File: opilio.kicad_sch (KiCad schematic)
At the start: 24 parts, among them J1 Conn_01x04_Male, SW1 TS-1077S-01726, SW2 TS-1077S-01726, U1 STM32F103C8T6, Y1 YST310S 32.768KHz, Y2 TAXM8M4RFDCET2T

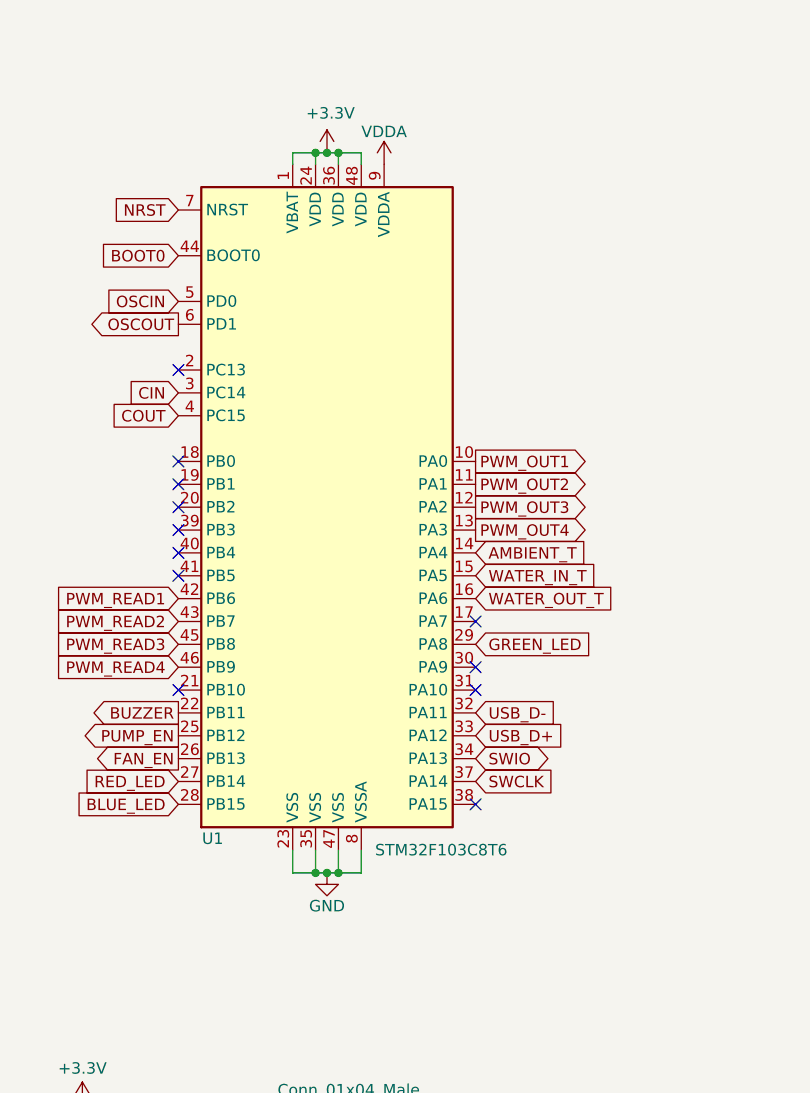
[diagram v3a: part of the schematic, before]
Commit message: wip migrate to kicad 7
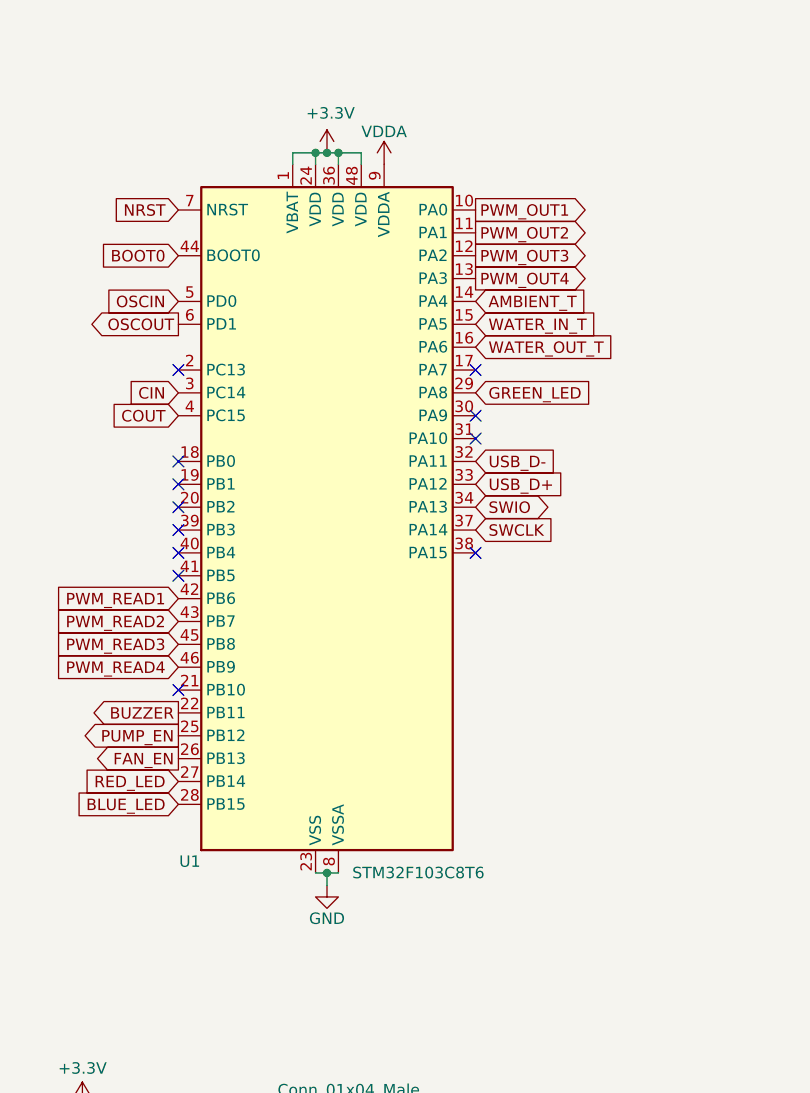
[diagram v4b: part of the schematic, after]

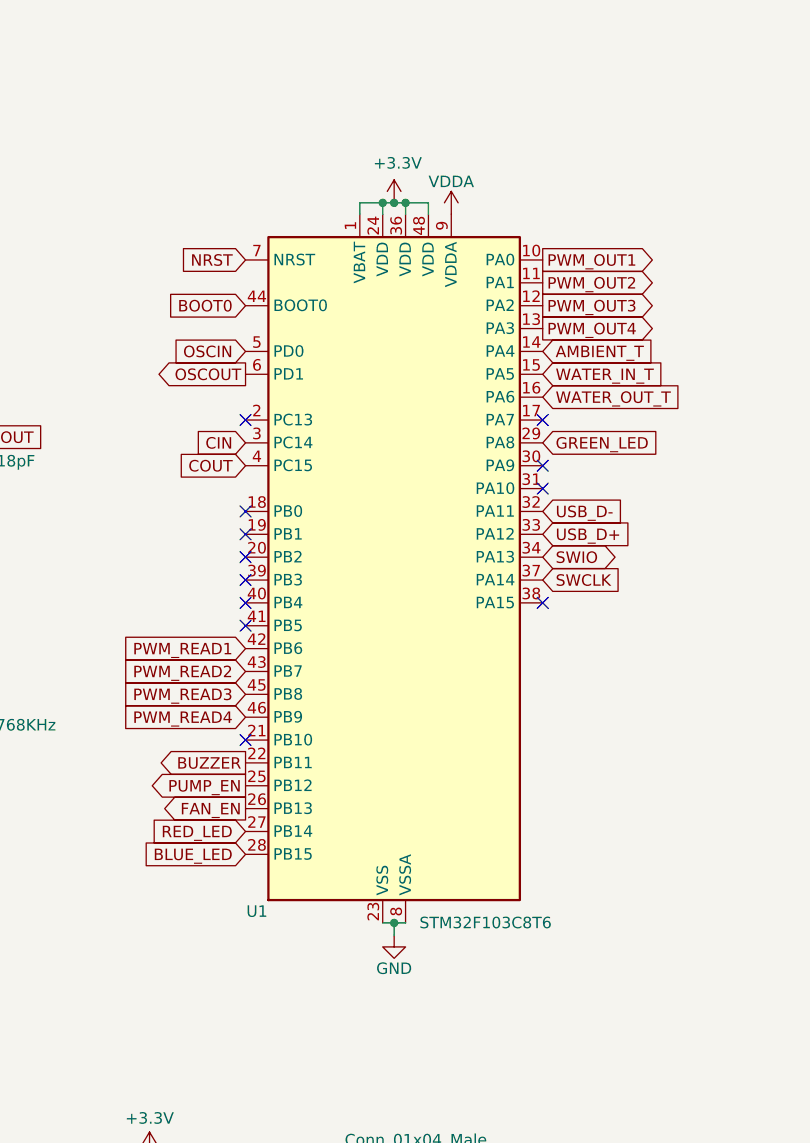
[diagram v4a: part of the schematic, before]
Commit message: migrated to kicad-7
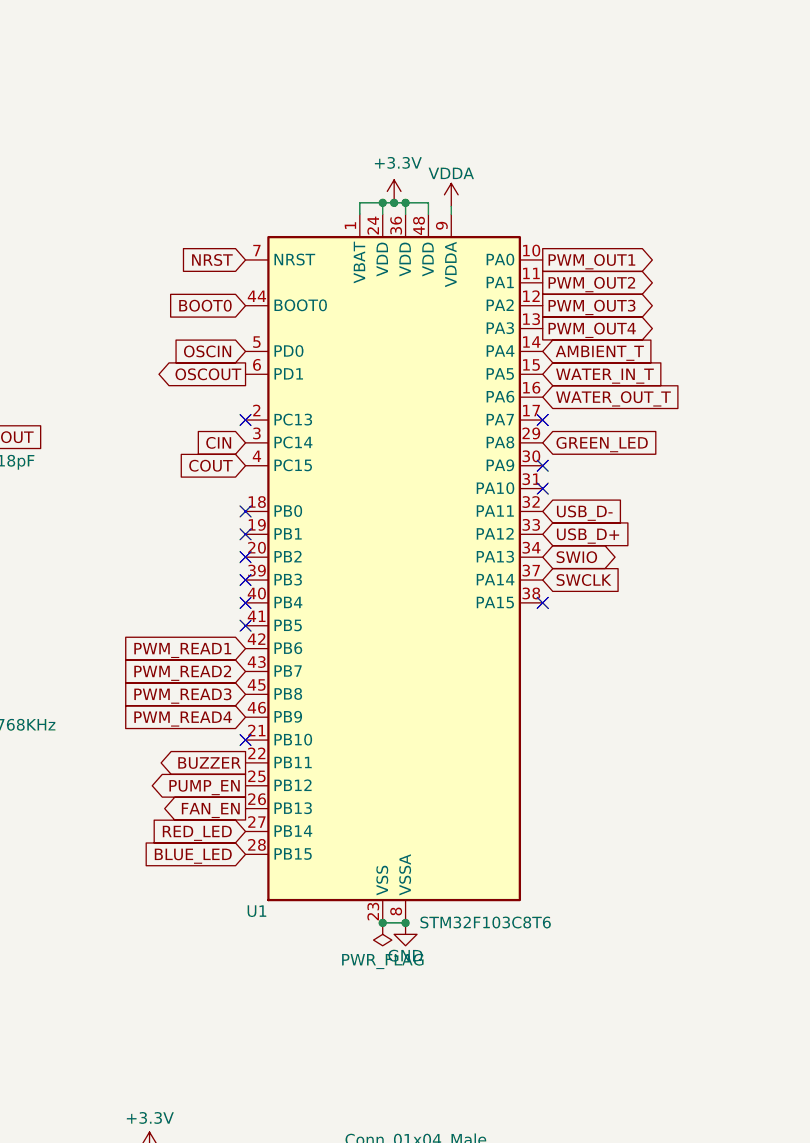
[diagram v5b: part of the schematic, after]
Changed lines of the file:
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@@
   (junction (at 118.999 61.976) (diameter 0) (color 0 0 0 0)
   )
+  (junction (at 118.999 141.986) (diameter 0) (color 0 0 0 0)
+  )
   (junction (at 51.181 118.999) (diameter 0) (color 0 0 0 0)
   )
   (junction (at 103.124 27.305) (diameter 0) (color 0 0 0 0)
   )
+  (junction (at 116.459 141.986) (diameter 0) (color 0 0 0 0)
+  )
   (junction (at 26.162 82.677) (diameter 0) (color 0 0 0 0)
   )
@@
   )
   (junction (at 29.591 51.181) (diameter 0) (color 0 0 0 0)
-  )
-  (junction (at 117.729 141.986) (diameter 0) (color 0 0 0 0)
   )
   (junction (at 31.242 78.613) (diameter 0) (color 0 0 0 0)
@@
     (stroke (width 0) (type default))
   )
-  (wire (pts (xy 116.459 141.986) (xy 117.729 141.986))
+  (wire (pts (xy 116.459 141.986) (xy 118.999 141.986))
     (stroke (width 0) (type default))
   )
@@
     (stroke (width 0) (type default))
   )
-  (wire (pts (xy 117.729 143.383) (xy 117.729 141.986))
-    (stroke (width 0) (type default))
-  )
   (wire (pts (xy 34.163 70.104) (xy 34.163 72.898))
     (stroke (width 0) (type default))
@@
     (stroke (width 0) (type default))
   )
+  (wire (pts (xy 124.079 62.357) (xy 124.079 63.246))
+    (stroke (width 0) (type default))
+  )
   (wire (pts (xy 21.082 73.533) (xy 21.082 70.104))
     (stroke (width 0) (type default))
@@
   )
   (wire (pts (xy 113.919 61.976) (xy 116.459 61.976))
-    (stroke (width 0) (type default))
-  )
-  (wire (pts (xy 117.729 141.986) (xy 118.999 141.986))
     (stroke (width 0) (type default))
   )
@@
         (path "/1fd8049d-01e3-48fd-a73a-49757ed6cc50"
           (reference "#PWR010") (unit 1)
+        )
+      )
+    )
+  )
+  (symbol (lib_id "power:PWR_FLAG") (at 116.459 141.986 180) (unit 1)
+    (in_bom yes) (on_board yes) (dnp no) (fields_autoplaced)
+    (property "Reference" "#FLG04" (at 116.459 143.891 0)
+      (effects (font (size 1.27 1.27)) hide)
+    )
+    (property "Value" "PWR_FLAG" (at 116.459 146.1215 0)
+      (effects (font (size 1.27 1.27)))
+    )
+    (property "Footprint" "" (at 116.459 141.986 0)
+      (effects (font (size 1.27 1.27)) hide)
+    )
+    (property "Datasheet" "~" (at 116.459 141.986 0)
+      (effects (font (size 1.27 1.27)) hide)
+    )
+    (pin "1")
+    (instances
+      (project "opilio"
+        (path "/1fd8049d-01e3-48fd-a73a-49757ed6cc50"
+          (reference "#FLG04") (unit 1)
         )
       )
@@
     )
   )
-  (symbol (lib_id "power:VDDA") (at 124.079 63.246 0) (unit 1)
+  (symbol (lib_id "power:VDDA") (at 124.079 62.357 0) (unit 1)
     (in_bom yes) (on_board yes) (dnp no) (fields_autoplaced)
-    (property "Reference" "#PWR013" (at 124.079 67.056 0)
-      (effects (font (size 1.27 1.27)) hide)
-    )
-    (property "Value" "VDDA" (at 124.079 59.6415 0)
-      (effects (font (size 1.27 1.27)))
-    )
-    (property "Footprint" "" (at 124.079 63.246 0)
-      (effects (font (size 1.27 1.27)) hide)
-    )
-    (property "Datasheet" "" (at 124.079 63.246 0)
+    (property "Reference" "#PWR013" (at 124.079 66.167 0)
+      (effects (font (size 1.27 1.27)) hide)
+    )
+    (property "Value" "VDDA" (at 124.079 58.7525 0)
+      (effects (font (size 1.27 1.27)))
+    )
+    (property "Footprint" "" (at 124.079 62.357 0)
+      (effects (font (size 1.27 1.27)) hide)
+    )
+    (property "Datasheet" "" (at 124.079 62.357 0)
       (effects (font (size 1.27 1.27)) hide)
     )
@@
     )
   )
-  (symbol (lib_id "power:GND") (at 117.729 143.383 0) (unit 1)
-    (in_bom yes) (on_board yes) (dnp no)
-    (property "Reference" "#PWR012" (at 117.729 149.733 0)
-      (effects (font (size 1.27 1.27)) hide)
-    )
-    (property "Value" "GND" (at 117.729 147.066 0)
-      (effects (font (size 1.27 1.27)))
-    )
-    (property "Footprint" "" (at 117.729 143.383 0)
-      (effects (font (size 1.27 1.27)) hide)
-    )
-    (property "Datasheet" "" (at 117.729 143.383 0)
-      (effects (font (size 1.27 1.27)) hide)
-    )
+  (symbol (lib_id "power:GND") (at 118.999 141.986 0) (unit 1)
+    (in_bom yes) (on_board yes) (dnp no)
+    (property "Reference" "#PWR012" (at 118.999 148.336 0)
+      (effects (font (size 1.27 1.27)) hide)
+    )
+    (property "Value" "GND" (at 118.999 145.669 0)
+      (effects (font (size 1.27 1.27)))
+    )
+    (property "Footprint" "" (at 118.999 141.986 0)
+      (effects (font (size 1.27 1.27)) hide)
+    )
+    (property "Datasheet" "" (at 118.999 141.986 0)
+      (effects (font (size 1.27 1.27)) hide)
+    )

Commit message: almost ready for order
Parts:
- added FID1, FID2, FID3: Fiducial, Fiducial:Fiducial_0.5mm_Mask1mm, symbol Mechanical:Fiducial
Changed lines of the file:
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@@
+    )
+  )
+  (symbol (lib_id "Mechanical:Fiducial") (at 24.257 149.733 0) (unit 1)
+    (in_bom yes) (on_board yes) (dnp no) (fields_autoplaced)
+    (property "Reference" "FID2" (at 26.416 149.0893 0)
+      (effects (font (size 1.27 1.27)) (justify left))
+    )
+    (property "Value" "Fiducial" (at 26.416 151.0103 0)
+      (effects (font (size 1.27 1.27)) (justify left))
+    )
+    (property "Footprint" "Fiducial:Fiducial_0.5mm_Mask1mm" (at 24.257 149.733 0)
+      (effects (font (size 1.27 1.27)) hide)
+    )
+    (property "Datasheet" "~" (at 24.257 149.733 0)
+      (effects (font (size 1.27 1.27)) hide)
+    )
+    (instances
+      (project "opilio"
+        (path "/1fd8049d-01e3-48fd-a73a-49757ed6cc50"
+          (reference "FID2") (unit 1)
+        )
+      )
     )
   )
@@
     )
   )
+  (symbol (lib_id "Mechanical:Fiducial") (at 24.13 145.288 0) (unit 1)
+    (in_bom yes) (on_board yes) (dnp no) (fields_autoplaced)
+    (property "Reference" "FID1" (at 26.289 144.6443 0)
+      (effects (font (size 1.27 1.27)) (justify left))
+    )
+    (property "Value" "Fiducial" (at 26.289 146.5653 0)
+      (effects (font (size 1.27 1.27)) (justify left))
+    )
+    (property "Footprint" "Fiducial:Fiducial_0.5mm_Mask1mm" (at 24.13 145.288 0)
+      (effects (font (size 1.27 1.27)) hide)
+    )
+    (property "Datasheet" "~" (at 24.13 145.288 0)
+      (effects (font (size 1.27 1.27)) hide)
+    )
+    (instances
+      (project "opilio"
+        (path "/1fd8049d-01e3-48fd-a73a-49757ed6cc50"
+          (reference "FID1") (unit 1)
+        )
+      )
+    )
+  )
   (symbol (lib_id "Graphic:Logo_Open_Hardware_Small") (at 22.098 187.579 0) (unit 1)
     (in_bom yes) (on_board yes) (dnp no) (fields_autoplaced)
@@
         )
       )
+    )
+  )
+  (symbol (lib_id "Mechanical:Fiducial") (at 24.511 154.432 0) (unit 1)
+    (in_bom yes) (on_board yes) (dnp no) (fields_autoplaced)
+    (property "Reference" "FID3" (at 26.67 153.7883 0)
+      (effects (font (size 1.27 1.27)) (justify left))
+    )
+    (property "Value" "Fiducial" (at 26.67 155.7093 0)
+      (effects (font (size 1.27 1.27)) (justify left))
+    )
+    (property "Footprint" "Fiducial:Fiducial_0.5mm_Mask1mm" (at 24.511 154.432 0)
+      (effects (font (size 1.27 1.27)) hide)
+    )
+    (property "Datasheet" "~" (at 24.511 154.432 0)
+      (effects (font (size 1.27 1.27)) hide)
+    )
+    (instances
+      (project "opilio"
+        (path "/1fd8049d-01e3-48fd-a73a-49757ed6cc50"
+          (reference "FID3") (unit 1)
+        )
+      )
